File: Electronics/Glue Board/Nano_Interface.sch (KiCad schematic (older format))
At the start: 1 part, among them U5 ISO1540

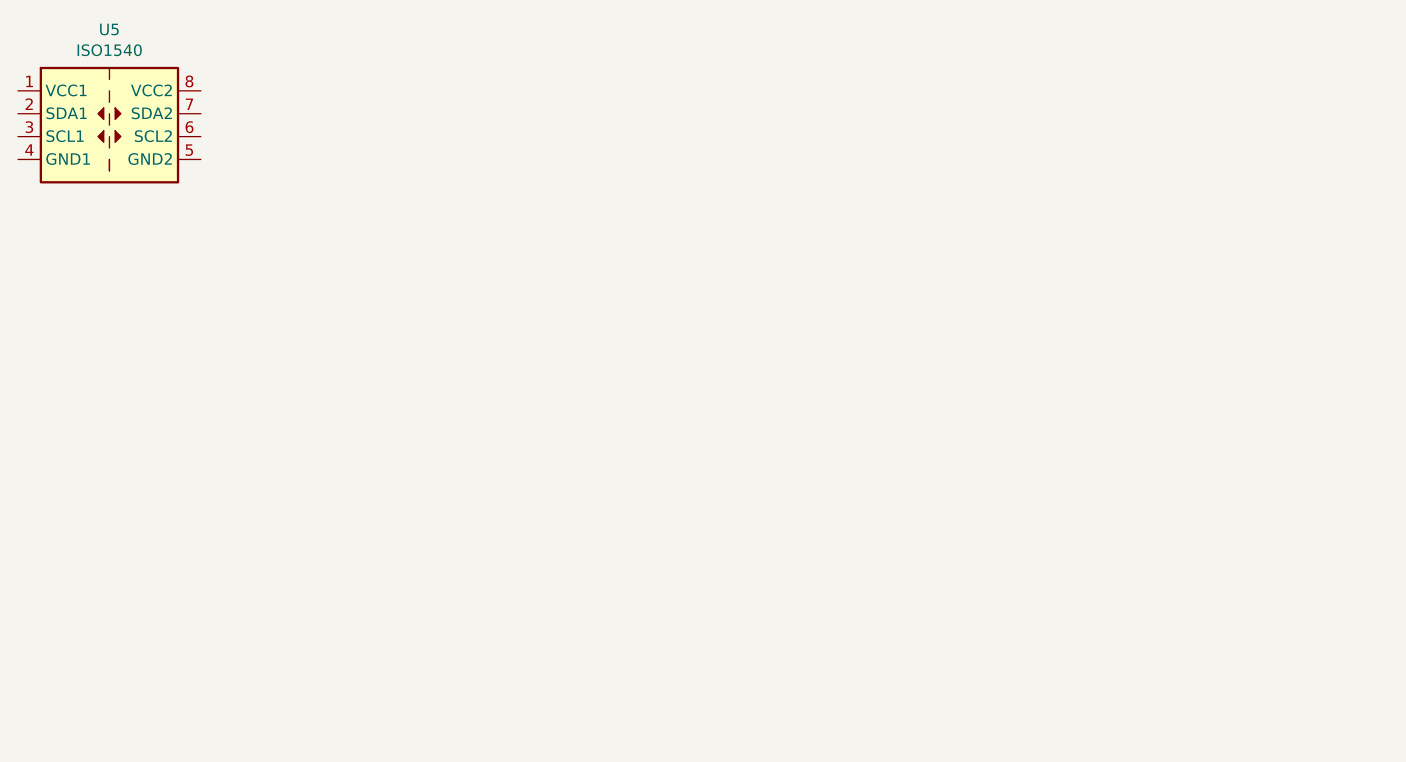
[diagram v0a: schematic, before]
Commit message: Finished the schematic for the most parts
Finished the schematic for the most parts
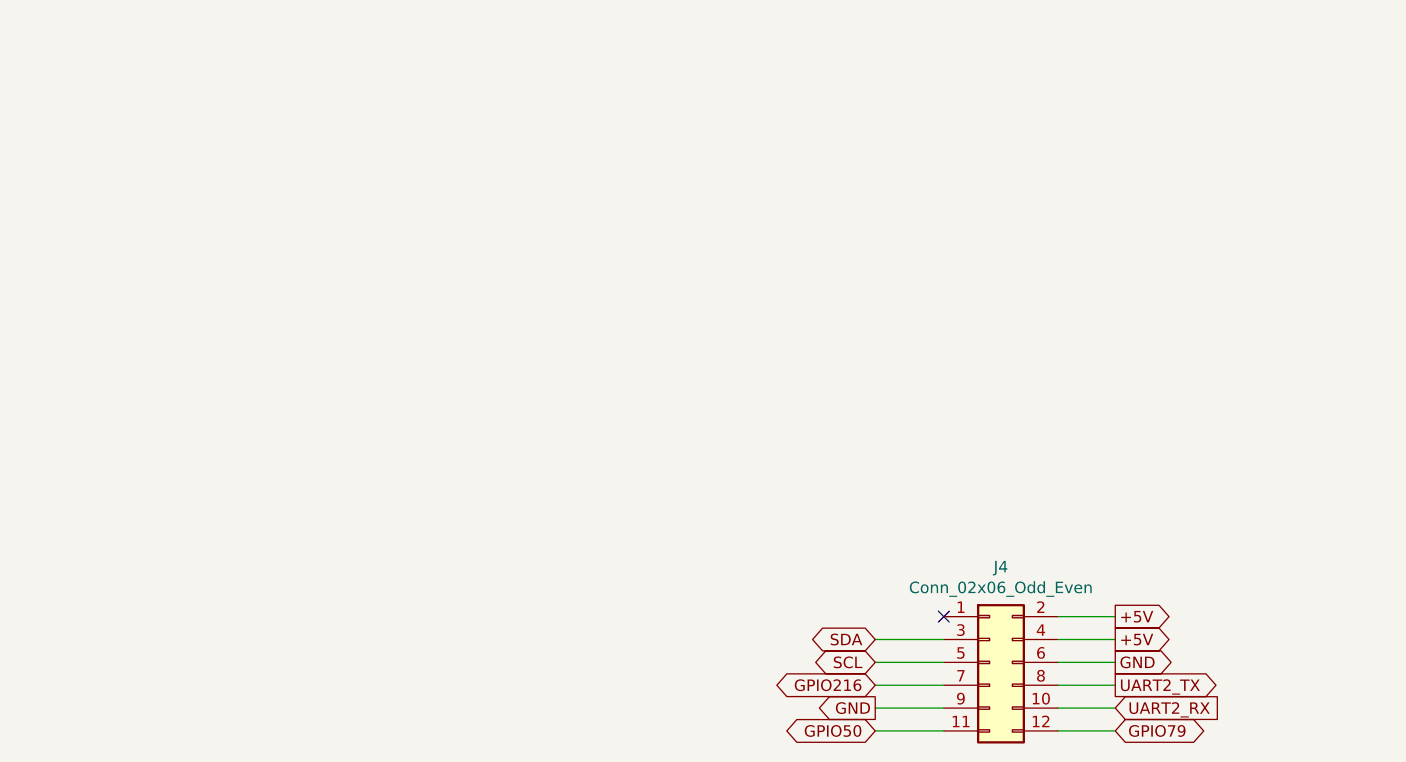
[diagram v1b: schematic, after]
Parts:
- removed U5: ISO1540, Package_SO:SOIC-8_3.9x4.9mm_P1.27mm, symbol Isolator:ISO1540
- added J4: Conn_02x06_Odd_Even, Connector_PinHeader_2.54mm:PinHeader_2x06_P2.54mm_Vertical, symbol Connector_Generic:Conn_02x06_Odd_Even
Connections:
- new net +5V: J4.2 (Pin_2), J4.4 (Pin_4)
- new net GND: J4.6 (Pin_6), J4.9 (Pin_9)
- new net GPIO216: J4.7 (Pin_7)
- new net GPIO50: J4.11 (Pin_11)
- new net GPIO79: J4.12 (Pin_12)
- new net SCL: J4.5 (Pin_5)
- new net SDA: J4.3 (Pin_3)
- new net UART2_RX: J4.10 (Pin_10)
- new net UART2_TX: J4.8 (Pin_8)
- no-connect marks 0 -> 1
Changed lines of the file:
@@
 EELAYER 30 0
 EELAYER END
-$Descr A4 11693 8268
+$Descr B 17000 11000
 encoding utf-8
 Sheet 5 5
@@
 $EndDescr
 $Comp
-L Isolator:ISO1540 U5
-U 1 1 5E0733D7
-P 4450 2700
-F 0 "U5" H 4450 3067 50  0000 C CNN
-F 1 "ISO1540" H 4450 2976 50  0000 C CNN
-F 2 "Package_SO:SOIC-8_3.9x4.9mm_P1.27mm" H 4450 2350 50  0001 C CNN
-F 3 "http://www.ti.com/lit/ds/symlink/iso1541.pdf" H 4450 2750 50  0001 C CNN
-	1    4450 2700
+L Connector_Generic:Conn_02x06_Odd_Even J4
+U 1 1 5E1CE768
+P 8300 5100
+F 0 "J4" H 8350 5517 50  0000 C CNN
+F 1 "Conn_02x06_Odd_Even" H 8350 5426 50  0000 C CNN
+F 2 "Connector_PinHeader_2.54mm:PinHeader_2x06_P2.54mm_Vertical" H 8300 5100 50  0001 C CNN
+F 3 "~" H 8300 5100 50  0001 C CNN
+	1    8300 5100
 	1    0    0    -1
 $EndComp
+Text GLabel 8850 4900 2    50   Output ~ 0
++5V
+Text GLabel 8850 5000 2    50   Output ~ 0
++5V
+Wire Wire Line
+	8600 4900 8850 4900
+Wire Wire Line
+	8600 5000 8850 5000
+Text GLabel 8850 5100 2    50   Output ~ 0
+GND
+Text GLabel 7800 5300 0    50   Output ~ 0
+GND
+Wire Wire Line
+	8600 5100 8850 5100
+Wire Wire Line
+	7800 5300 8100 5300
+Text GLabel 7800 5000 0    50   BiDi ~ 0
+SDA
+Text GLabel 7800 5100 0    50   BiDi ~ 0
+SCL
+Text GLabel 7800 5200 0    50   BiDi ~ 0
+GPIO216
+Text GLabel 7800 5400 0    50   BiDi ~ 0
+GPIO50
+Text GLabel 8850 5400 2    50   BiDi ~ 0
+GPIO79
+Wire Wire Line
+	7800 5000 8100 5000
+Wire Wire Line
+	7800 5100 8100 5100
+Wire Wire Line
+	7800 5200 8100 5200
+Wire Wire Line
+	8100 5400 7800 5400
+Wire Wire Line
+	8600 5400 8850 5400
+Text GLabel 8850 5200 2    50   Output ~ 0
+UART2_TX
+Text GLabel 8850 5300 2    50   Input ~ 0
+UART2_RX
+NoConn ~ 8100 4900
+Wire Wire Line
+	8600 5200 8850 5200
+Wire Wire Line
+	8850 5300 8600 5300
 $EndSCHEMATC

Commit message: Complete Schematic and BOM
Complete Schematic and BOM. Next up, layout!
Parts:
- J4: MPN (none) -> 67997-112HLF
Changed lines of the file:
@@
 encoding utf-8
 Sheet 5 5
-Title ""
-Date ""
-Rev ""
+Title "Robocar, Pinky, Nano Interface"
+Date "2019-12-28"
+Rev "A"
 Comp ""
 Comment1 ""
@@
 F 2 "Connector_PinHeader_2.54mm:PinHeader_2x06_P2.54mm_Vertical" H 8300 5100 50  0001 C CNN
 F 3 "~" H 8300 5100 50  0001 C CNN
+F 4 "67997-112HLF" H 8300 5100 50  0001 C CNN "MPN"
 	1    8300 5100
 	1    0    0    -1

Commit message: Added Motor v-sense and battery mon. Layout time!
Added Motor v-sense and battery mon. Layout time!
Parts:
- added J7: Conn_01x04_Male, Connector_PinHeader_2.54mm:PinHeader_1x04_P2.54mm_Vertical, symbol Connector:Conn_01x04_Male
- added J8: Conn_02x03_Odd_Even, Connector_IDC:IDC-Header_2x03_P2.54mm_Vertical, symbol Connector_Generic:Conn_02x03_Odd_Even
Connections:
- net +5V: now also J7.1 (Pin_1)
- net GND: now also J7.2 (Pin_2), J8.6 (Pin_6)
- net GPIO50: now also J8.1 (Pin_1)
- net GPIO79: now also J8.2 (Pin_2)
- net SCL: now also J7.4 (Pin_4), J8.4 (Pin_4)
- net SDA: now also J7.3 (Pin_3), J8.3 (Pin_3)
- net +3.3V: now reaches J4.1 (Pin_1)
- net +3.3V: now also J8.5 (Pin_5)
- no-connect marks 1 -> 0
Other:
- note added: "SHITTY ADD-ON\nV. 1.69BIS\nCOMPLIANT"
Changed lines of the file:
@@
 	1    0    0    -1
 $EndComp
-Text GLabel 8850 4900 2    50   Output ~ 0
+Text GLabel 8850 4900 2    50   Input ~ 0
 +5V
-Text GLabel 8850 5000 2    50   Output ~ 0
+Text GLabel 8850 5000 2    50   Input ~ 0
 +5V
 Wire Wire Line
@@
 Wire Wire Line
 	8600 5000 8850 5000
-Text GLabel 8850 5100 2    50   Output ~ 0
+Text GLabel 8850 5100 2    50   Input ~ 0
 GND
-Text GLabel 7800 5300 0    50   Output ~ 0
+Text GLabel 7800 5300 0    50   Input ~ 0
 GND
 Wire Wire Line
@@
 Text GLabel 8850 5300 2    50   Input ~ 0
 UART2_RX
-NoConn ~ 8100 4900
 Wire Wire Line
 	8600 5200 8850 5200
 Wire Wire Line
 	8850 5300 8600 5300
+Text GLabel 8850 3500 2    50   BiDi ~ 0
+SDA
+Text GLabel 7800 3500 0    50   BiDi ~ 0
+SCL
+Text GLabel 7800 3400 0    50   Input ~ 0
+GND
+Text GLabel 7800 4900 0    50   Output ~ 0
++3.3V
+Wire Wire Line
+	8100 4900 7800 4900
+$Comp
+L Connector:Conn_01x04_Male J7
+U 1 1 5E13F760
+P 8200 4250
+F 0 "J7" H 8308 4531 50  0000 C CNN
+F 1 "Conn_01x04_Male" H 8308 4440 50  0000 C CNN
+F 2 "Connector_PinHeader_2.54mm:PinHeader_1x04_P2.54mm_Vertical" H 8200 4250 50  0001 C CNN
+F 3 "~" H 8200 4250 50  0001 C CNN
+	1    8200 4250
+	1    0    0    -1
+$EndComp
+Text GLabel 8850 4150 2    50   Input ~ 0
++5V
+Text GLabel 8850 4250 2    50   Input ~ 0
+GND
+Text GLabel 8850 3600 2    50   BiDi ~ 0
+GPIO50
+Text GLabel 7800 3600 0    50   BiDi ~ 0
+GPIO79
+Text GLabel 8850 3400 2    50   Input ~ 0
++3.3V
+$Comp
+L Connector_Generic:Conn_02x03_Odd_Even J8
+U 1 1 5E141539
+P 8400 3500
+F 0 "J8" H 8450 3175 50  0000 C CNN
+F 1 "Conn_02x03_Odd_Even" H 8450 3266 50  0000 C CNN
+F 2 "Connector_IDC:IDC-Header_2x03_P2.54mm_Vertical" H 8400 3500 50  0001 C CNN
+F 3 "~" H 8400 3500 50  0001 C CNN
+F 4 "SFH11-NBPC-D03-ST-BK" H 8400 3500 50  0001 C CNN "MPN"
+	1    8400 3500
+	-1   0    0    1
+$EndComp
+Wire Wire Line
+	7800 3400 8100 3400
+Wire Wire Line
+	8100 3500 7800 3500
+Wire Wire Line
+	7800 3600 8100 3600
+Wire Wire Line
+	8600 3400 8850 3400
+Wire Wire Line
+	8850 3500 8600 3500
+Wire Wire Line
+	8600 3600 8850 3600
+Wire Wire Line
+	8400 4150 8850 4150
+Wire Wire Line
+	8850 4250 8400 4250
+Text GLabel 8850 4350 2    50   BiDi ~ 0
+SDA
+Text GLabel 8850 4450 2    50   BiDi ~ 0
+SCL
+Wire Wire Line
+	8850 4350 8400 4350
+Wire Wire Line
+	8400 4450 8850 4450
+Text Notes 9350 3600 0    50   ~ 0
+SHITTY ADD-ON\nV. 1.69BIS\nCOMPLIANT
 $EndSCHEMATC
